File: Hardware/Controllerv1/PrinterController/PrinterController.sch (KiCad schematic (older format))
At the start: 0 parts

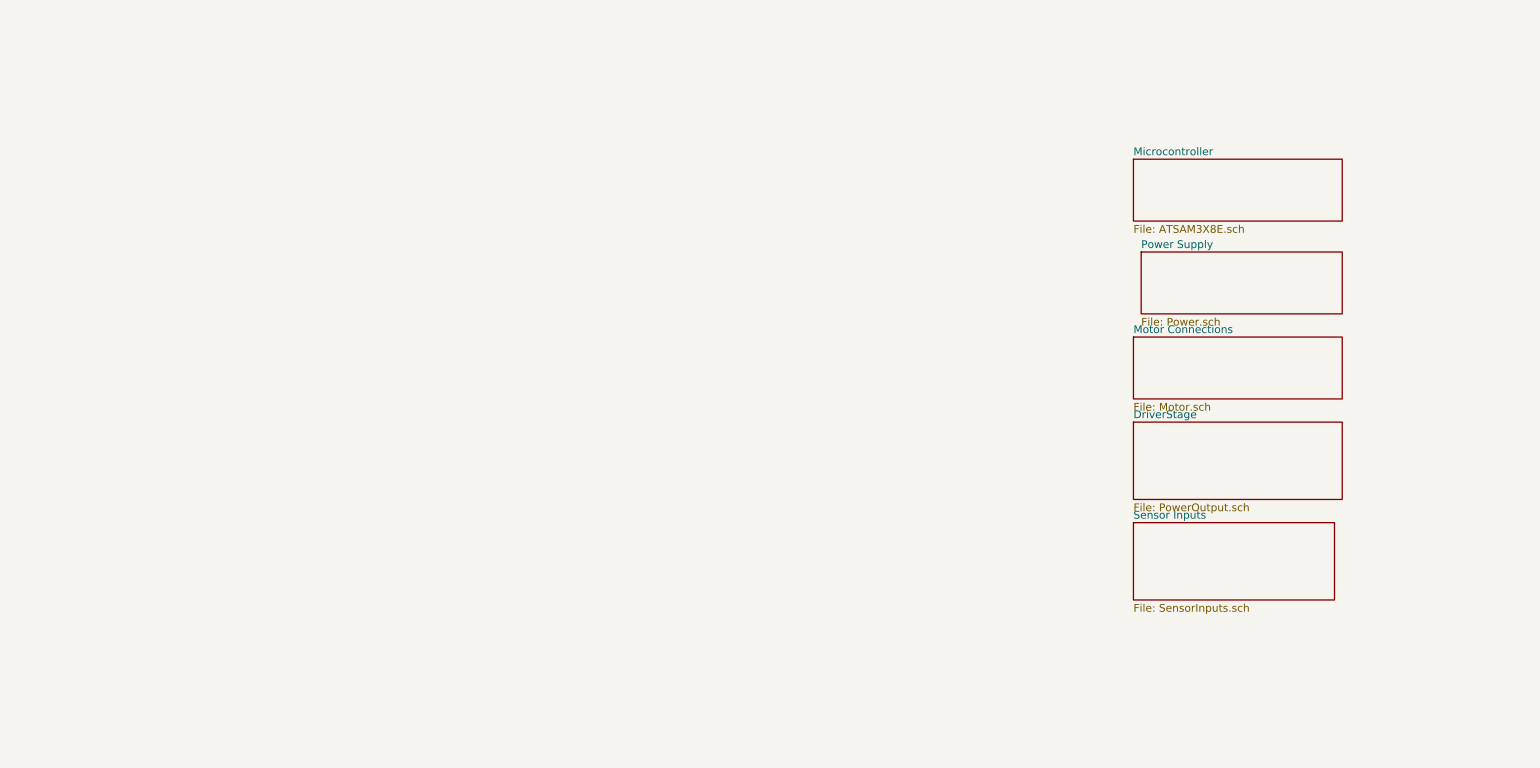
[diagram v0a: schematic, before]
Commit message: Added main controller and Power Outputs
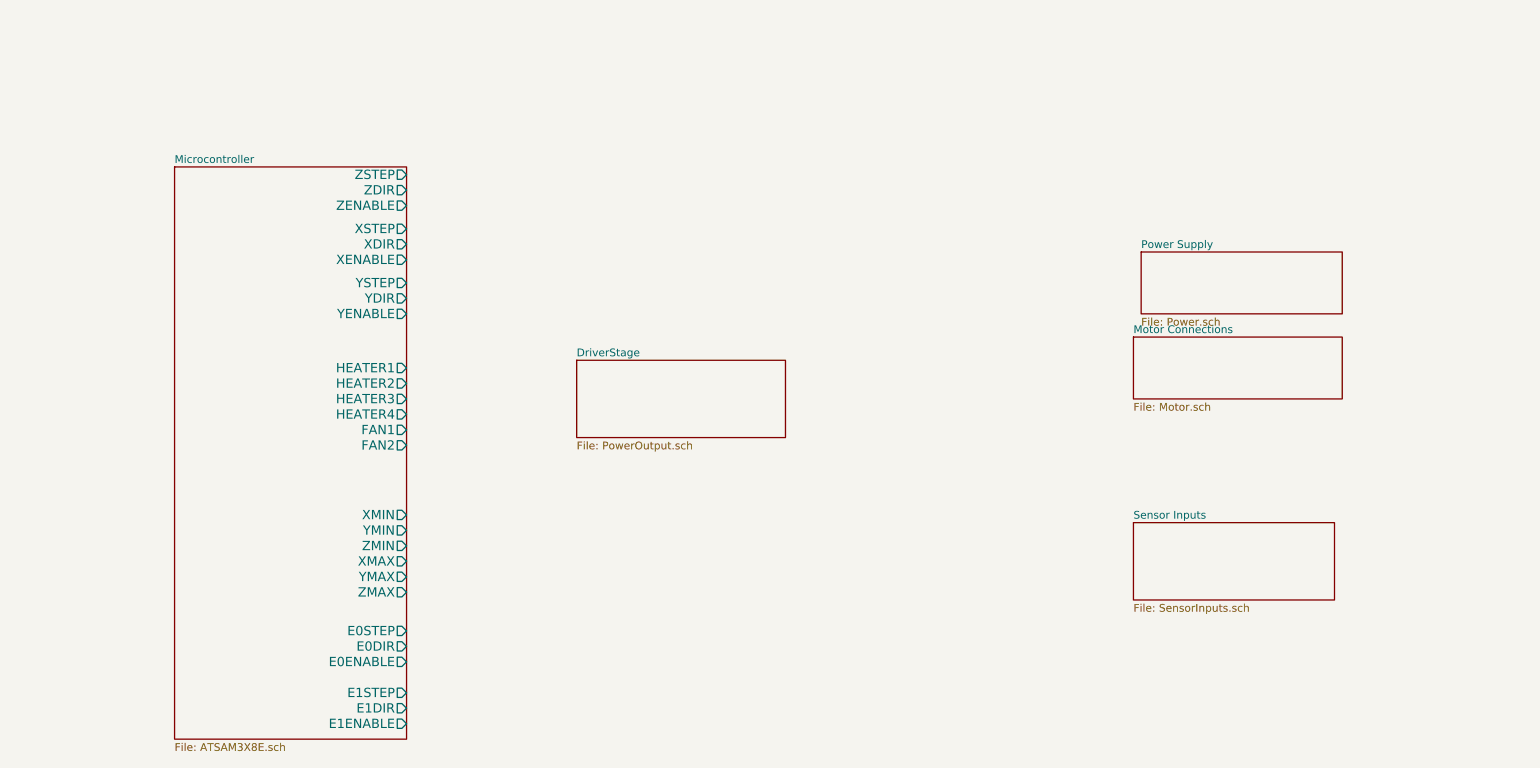
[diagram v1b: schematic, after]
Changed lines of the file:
@@
-EESchema Schematic File Version 4
-EELAYER 26 0
+EESchema Schematic File Version 2
+LIBS:74xgxx
+LIBS:74xx
+LIBS:ac-dc
+LIBS:actel
+LIBS:adc-dac
+LIBS:allegro
+LIBS:Altera
+LIBS:analog_devices
+LIBS:analog_switches
+LIBS:atmel
+LIBS:audio
+LIBS:battery_management
+LIBS:bbd
+LIBS:bosch
+LIBS:brooktre
+LIBS:cmos_ieee
+LIBS:cmos4000
+LIBS:conn
+LIBS:contrib
+LIBS:cypress
+LIBS:dc-dc
+LIBS:device
+LIBS:digital-audio
+LIBS:diode
+LIBS:display
+LIBS:dsp
+LIBS:elec-unifil
+LIBS:ESD_Protection
+LIBS:ftdi
+LIBS:gennum
+LIBS:graphic_symbols
+LIBS:hc11
+LIBS:infineon
+LIBS:intel
+LIBS:interface
+LIBS:intersil
+LIBS:ir
+LIBS:Lattice
+LIBS:leds
+LIBS:LEM
+LIBS:linear
+LIBS:logic_programmable
+LIBS:maxim
+LIBS:mechanical
+LIBS:memory
+LIBS:microchip
+LIBS:microchip_dspic33dsc
+LIBS:microchip_pic10mcu
+LIBS:microchip_pic12mcu
+LIBS:microchip_pic16mcu
+LIBS:microchip_pic18mcu
+LIBS:microchip_pic24mcu
+LIBS:microchip_pic32mcu
+LIBS:microcontrollers
+LIBS:modules
+LIBS:motor_drivers
+LIBS:motorola
+LIBS:motors
+LIBS:msp430
+LIBS:nordicsemi
+LIBS:nxp
+LIBS:nxp_armmcu
+LIBS:onsemi
+LIBS:opto
+LIBS:Oscillators
+LIBS:philips
+LIBS:power
+LIBS:Power_Management
+LIBS:powerint
+LIBS:pspice
+LIBS:references
+LIBS:regul
+LIBS:relays
+LIBS:rfcom
+LIBS:RFSolutions
+LIBS:sensors
+LIBS:silabs
+LIBS:siliconi
+LIBS:stm8
+LIBS:stm32
+LIBS:supertex
+LIBS:switches
+LIBS:texas
+LIBS:transf
+LIBS:transistors
+LIBS:triac_thyristor
+LIBS:ttl_ieee
+LIBS:valves
+LIBS:video
+LIBS:wiznet
+LIBS:Worldsemi
+LIBS:Xicor
+LIBS:xilinx
+LIBS:zetex
+LIBS:Zilog
+LIBS:PrinterController-cache
+EELAYER 25 0
 EELAYER END
 $Descr A4 11693 8268
@@
 $EndDescr
 $Sheet
-S 8500 1350 1350 400
+S 2300 1400 1500 3700
 U 5B2631DE
 F0 "Microcontroller" 50
 F1 "ATSAM3X8E.sch" 50
+F2 "ZSTEP" O R 3800 1450 60
+F3 "ZDIR" O R 3800 1550 60
+F4 "XSTEP" O R 3800 1800 60
+F5 "XDIR" O R 3800 1900 60
+F6 "YSTEP" O R 3800 2150 60
+F7 "YDIR" O R 3800 2250 60
+F8 "XENABLE" O R 3800 2000 60
+F9 "YENABLE" O R 3800 2350 60
+F10 "ZENABLE" O R 3800 1650 60
+F11 "HEATER2" O R 3800 2800 60
+F12 "HEATER1" O R 3800 2700 60
+F13 "HEATER3" O R 3800 2900 60
+F14 "HEATER4" O R 3800 3000 60
+F15 "FAN1" O R 3800 3100 60
+F16 "FAN2" O R 3800 3200 60
+F17 "XMIN" O R 3800 3650 60
+F18 "YMIN" O R 3800 3750 60
+F19 "ZMIN" O R 3800 3850 60
+F20 "XMAX" O R 3800 3950 60
+F21 "YMAX" O R 3800 4050 60
+F22 "ZMAX" O R 3800 4150 60
+F23 "E0DIR" O R 3800 4500 60
+F24 "E0STEP" O R 3800 4400 60
+F25 "E0ENABLE" O R 3800 4600 60
+F26 "E1STEP" O R 3800 4800 60
+F27 "E1DIR" O R 3800 4900 60
+F28 "E1ENABLE" O R 3800 5000 60
 $EndSheet
 $Sheet
@@
 $EndSheet
 $Sheet
-S 8500 3050 1350 500
+S 4900 2650 1350 500
 U 5B26C5C4
 F0 "DriverStage" 50

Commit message: Added updates to PCB
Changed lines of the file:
@@
 LIBS:zetex
 LIBS:Zilog
+LIBS:IRFR3711TRPBF
 LIBS:PrinterController-cache
 EELAYER 25 0
@@
 $EndSheet
 $Sheet
-S 8500 2500 1350 400
+S 5550 600  800  2000
 U 5B26C5B2
 F0 "Motor Connections" 50
 F1 "Motor.sch" 50
+F2 "XENABLE" I L 5550 1350 60
+F3 "XSTEP" I L 5550 1150 60
+F4 "XDIR" I L 5550 1250 60
+F5 "YENABLE" I L 5550 1800 60
+F6 "YSTEP" I L 5550 1600 60
+F7 "YDIR" I L 5550 1700 60
+F8 "ZENABLE" I L 5550 950 60
+F9 "ZSTEP" I L 5550 750 60
+F10 "ZDIR" I L 5550 850 60
+F11 "E0ENABLE" I L 5550 2150 60
+F12 "E0STEP" I L 5550 1950 60
+F13 "E0DIR" I L 5550 2050 60
+F14 "E1ENABLE" I L 5550 2550 60
+F15 "E1STEP" I L 5550 2350 60
+F16 "E1DIR" I L 5550 2450 60
 $EndSheet
 $Sheet
-S 4900 2650 1350 500
+S 6450 2450 1400 1100
 U 5B26C5C4
 F0 "DriverStage" 50
 F1 "PowerOutput.sch" 50
+F2 "HEATER1" I L 6450 2700 60
+F3 "HEATER2" I L 6450 2800 60
+F4 "HEATER3" I L 6450 2900 60
+F5 "HEATER4" I L 6450 3000 60
+F6 "FAN1" I L 6450 3100 60
+F7 "FAN2" I L 6450 3200 60
 $EndSheet
 $Sheet
@@
 F1 "SensorInputs.sch" 50
 $EndSheet
+Wire Wire Line
+	3800 2700 6450 2700
+Wire Wire Line
+	3800 2800 6450 2800
+Wire Wire Line
+	3800 2900 6450 2900
+Wire Wire Line
+	3800 3000 6450 3000
+Wire Wire Line
+	3800 3100 6450 3100
+Wire Wire Line
+	3800 3200 6450 3200
+Wire Wire Line
+	4200 750  4200 1450
+Wire Wire Line
+	4200 1450 3800 1450
+Wire Wire Line
+	4250 1550 3800 1550
+Wire Wire Line
+	4250 850  4250 1550
+Wire Wire Line
+	4300 950  4300 1650
+Wire Wire Line
+	4300 1650 3800 1650
+Wire Wire Line
+	4350 1800 3800 1800
+Wire Wire Line
+	4350 1150 4350 1800
+Wire Wire Line
+	4400 1250 4400 1900
+Wire Wire Line
+	4400 1900 3800 1900
+Wire Wire Line
+	4550 2150 3800 2150
+Wire Wire Line
+	4550 1600 4550 2150
+Wire Wire Line
+	4600 1700 4600 2250
+Wire Wire Line
+	4600 2250 3800 2250
+Wire Wire Line
+	4650 2350 3800 2350
+Wire Wire Line
+	4650 1800 4650 2350
+Wire Wire Line
+	4450 1350 4450 2000
+Wire Wire Line
+	4450 2000 3800 2000
+Wire Wire Line
+	5550 750  4200 750
+Wire Wire Line
+	5550 850  4250 850
+Wire Wire Line
+	5550 950  4300 950
+Wire Wire Line
+	4350 1150 5550 1150
+Wire Wire Line
+	5550 1250 4400 1250
+Wire Wire Line
+	5550 1350 4450 1350
+Wire Wire Line
+	5550 1600 4550 1600
+Wire Wire Line
+	5550 1700 4600 1700
+Wire Wire Line
+	5550 1800 4650 1800
+Wire Wire Line
+	5550 1950 4800 1950
+Wire Wire Line
+	4800 1950 4800 4400
+Wire Wire Line
+	4800 4400 3800 4400
+Wire Wire Line
+	3800 4500 4850 4500
+Wire Wire Line
+	4850 4500 4850 2050
+Wire Wire Line
+	4850 2050 5550 2050
+Wire Wire Line
+	5550 2150 4900 2150
+Wire Wire Line
+	4900 2150 4900 4600
+Wire Wire Line
+	4900 4600 3800 4600
+Wire Wire Line
+	3800 4800 5000 4800
+Wire Wire Line
+	5000 4800 5000 2350
+Wire Wire Line
+	5000 2350 5550 2350
+Wire Wire Line
+	5550 2450 5050 2450
+Wire Wire Line
+	5050 2450 5050 4900
+Wire Wire Line
+	5050 4900 3800 4900
+Wire Wire Line
+	3800 5000 5100 5000
+Wire Wire Line
+	5100 5000 5100 2550
+Wire Wire Line
+	5100 2550 5550 2550
 $EndSCHEMATC

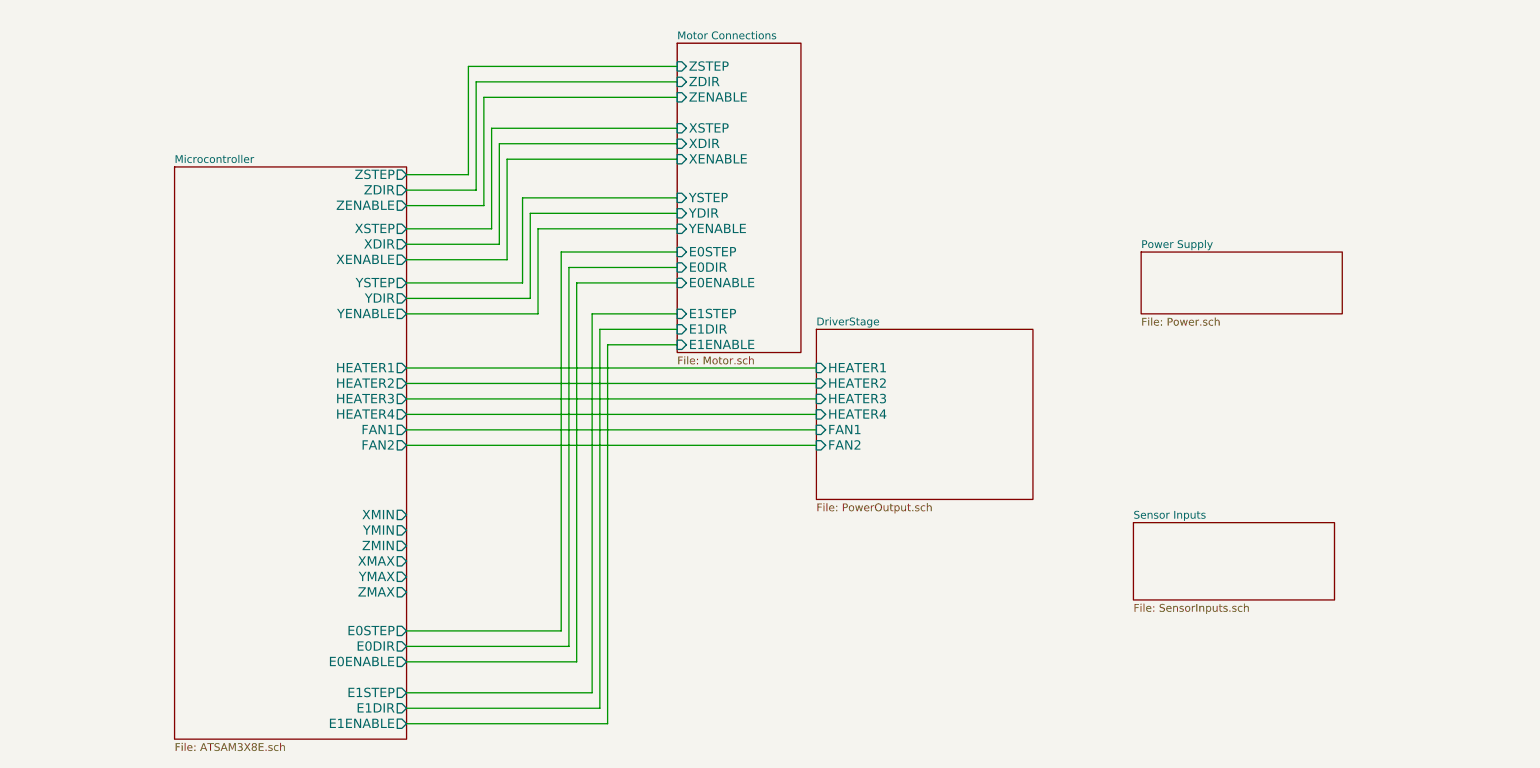
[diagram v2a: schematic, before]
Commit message: Added routed Power switching circuitry
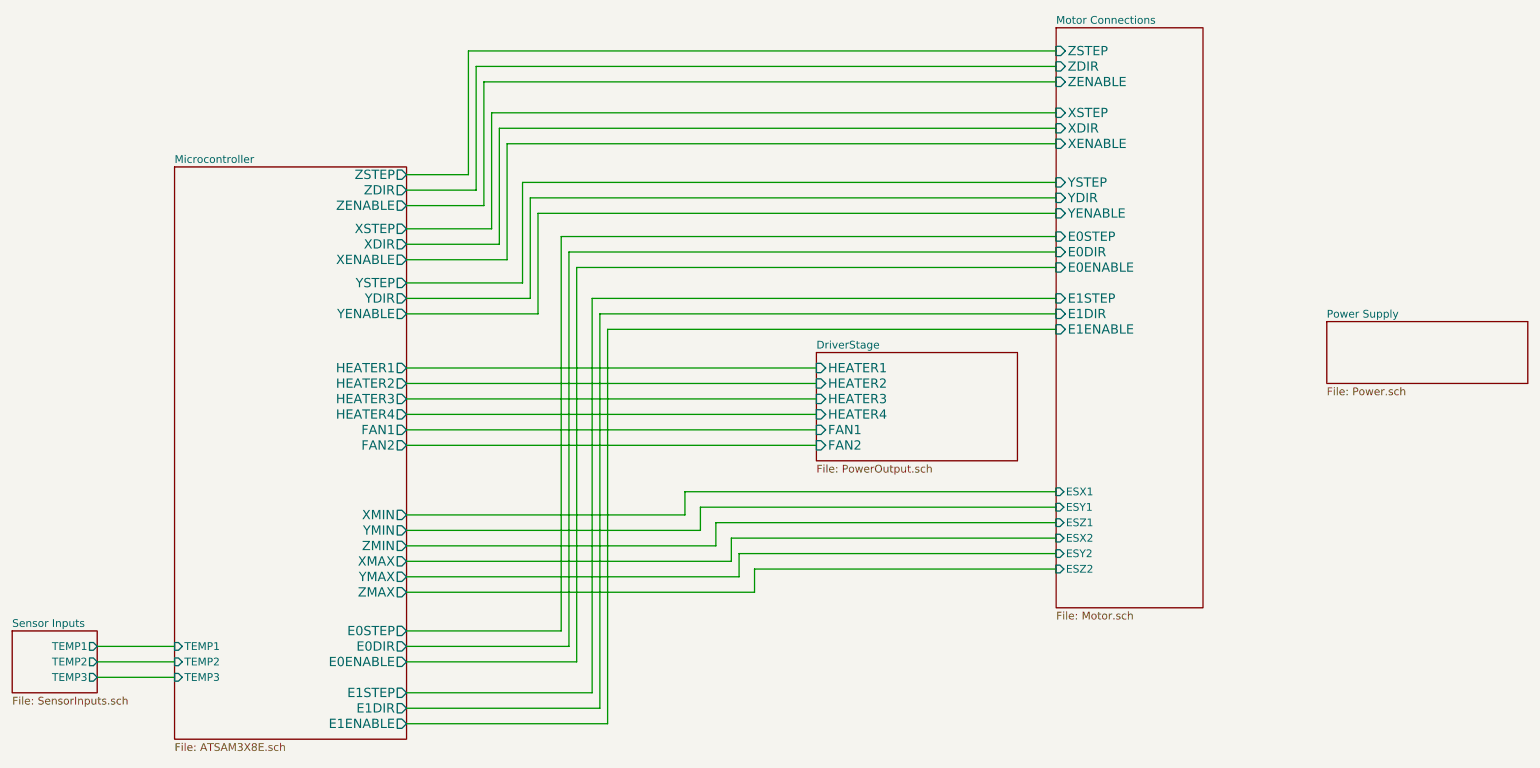
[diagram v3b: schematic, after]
